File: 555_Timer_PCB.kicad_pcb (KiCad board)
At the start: 2 copper layers, 50 x 40 mm, 9 parts, among them J1 Conn_01x02, U1 NE555P

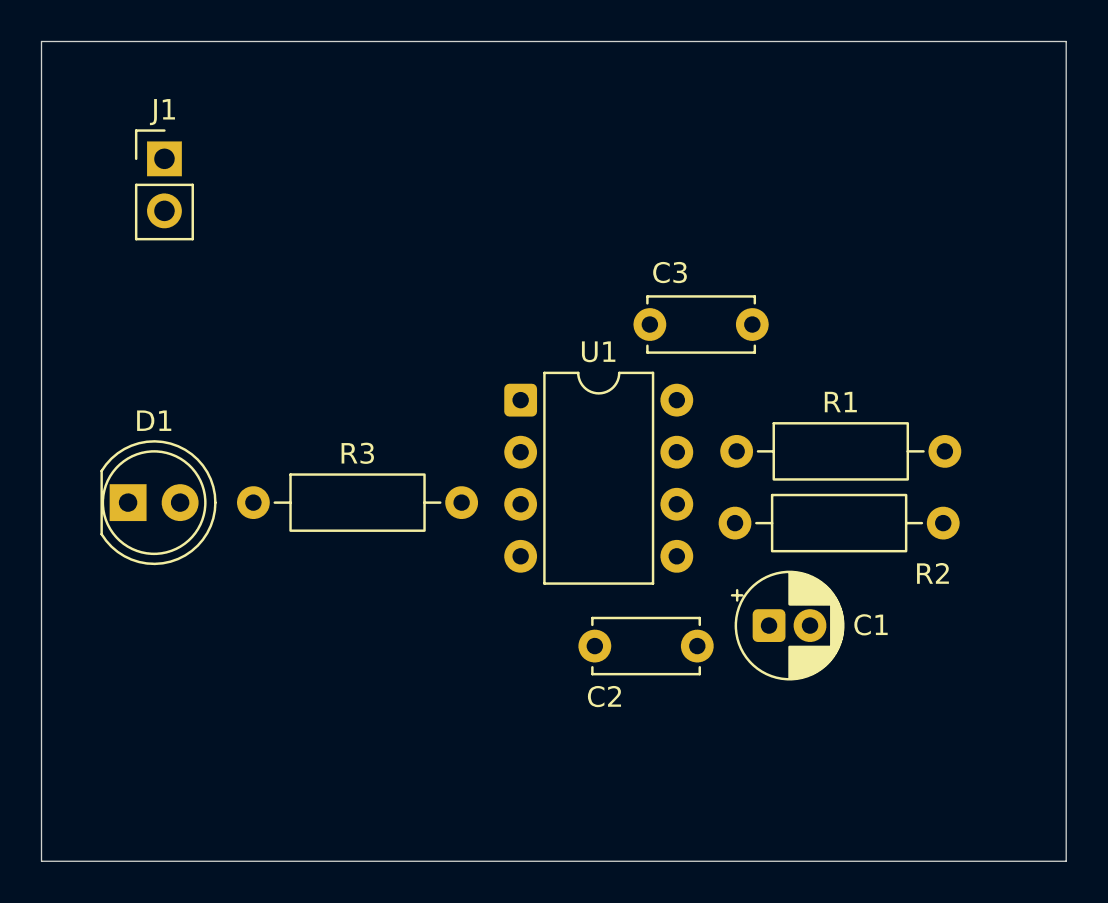
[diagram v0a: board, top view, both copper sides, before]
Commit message: Complete PCB routing and pass DRC
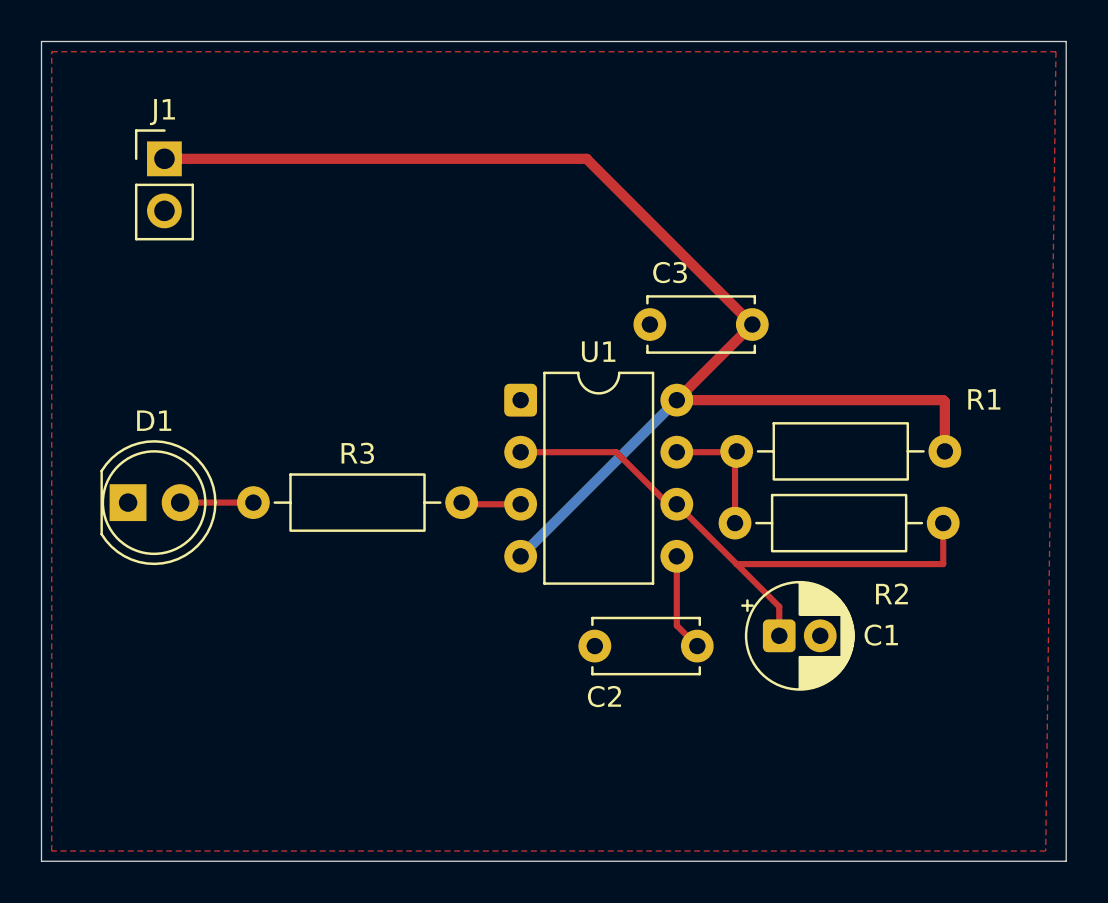
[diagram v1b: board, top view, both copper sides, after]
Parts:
- moved C1 0.71 mm to (204.0, 130.0)
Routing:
- net +5V: track 0.00 -> 63.7 mm
- net Net-(U1-THRES): track 0.00 -> 29.2 mm
- net Net-(U1-DISCH): track 0.00 -> 6.47 mm
- net Net-(U1-CONT): track 0.00 -> 4.79 mm
- net Net-(D1-A): track 0.00 -> 3.58 mm
- net Net-(U1-OUT): track 0.00 -> 2.91 mm
- added copper zone on F.Cu, net GND
